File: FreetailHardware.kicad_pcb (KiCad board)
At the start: 2 copper layers, 51.5 x 41 mm, 50 parts, among them CON1 Transducer, J1 TX, J2 REF, J3 RX, Q1 S8050, U1 Teensy3.2, U2 LMV324

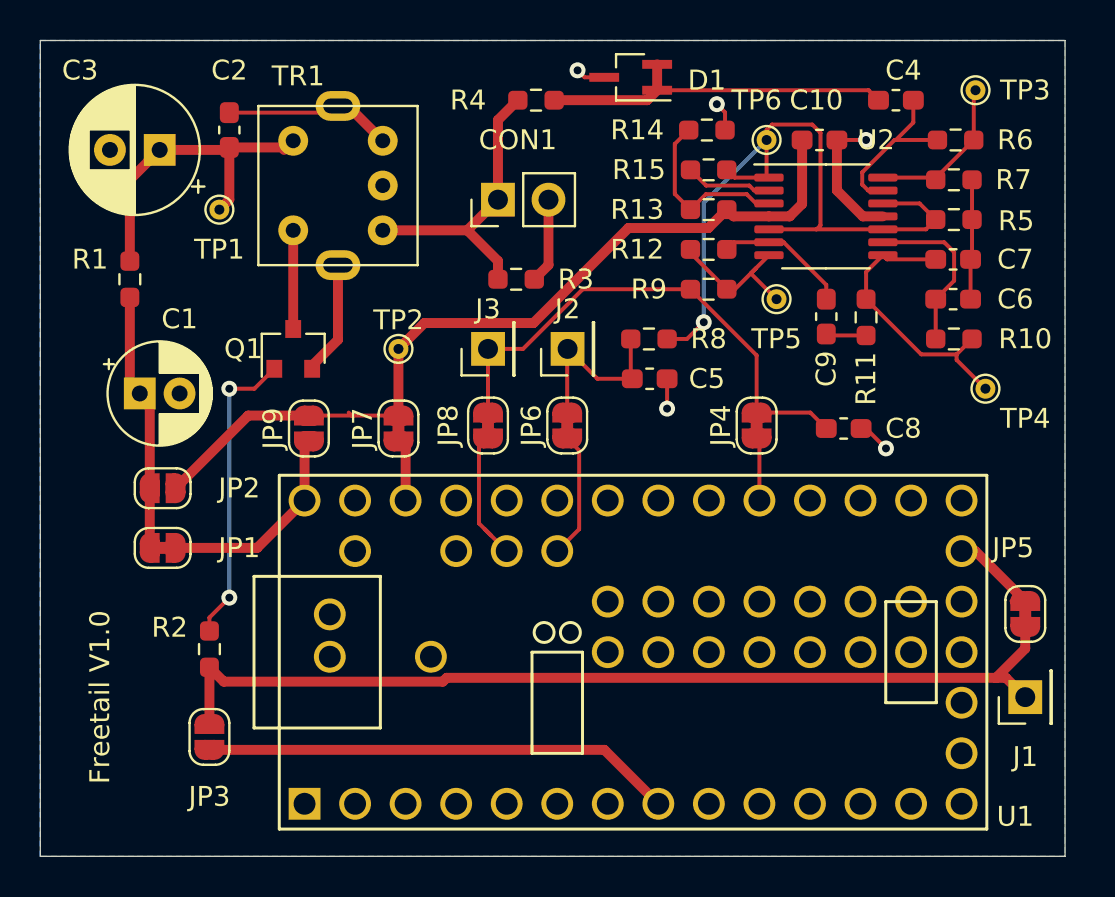
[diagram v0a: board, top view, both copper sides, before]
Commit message: Updated to KiCad v6
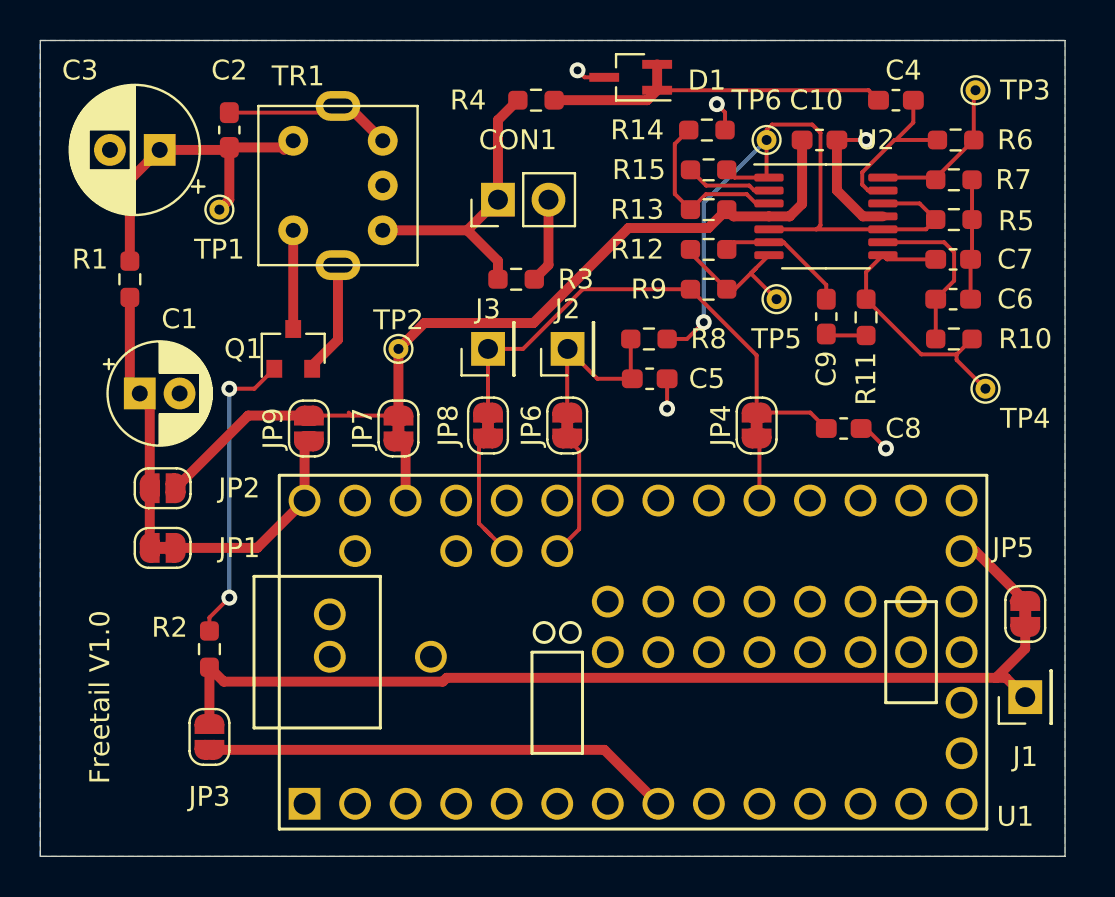
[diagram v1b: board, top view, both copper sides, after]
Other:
- net class Default removed

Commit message: v1.1 Hardware sent for fabrication
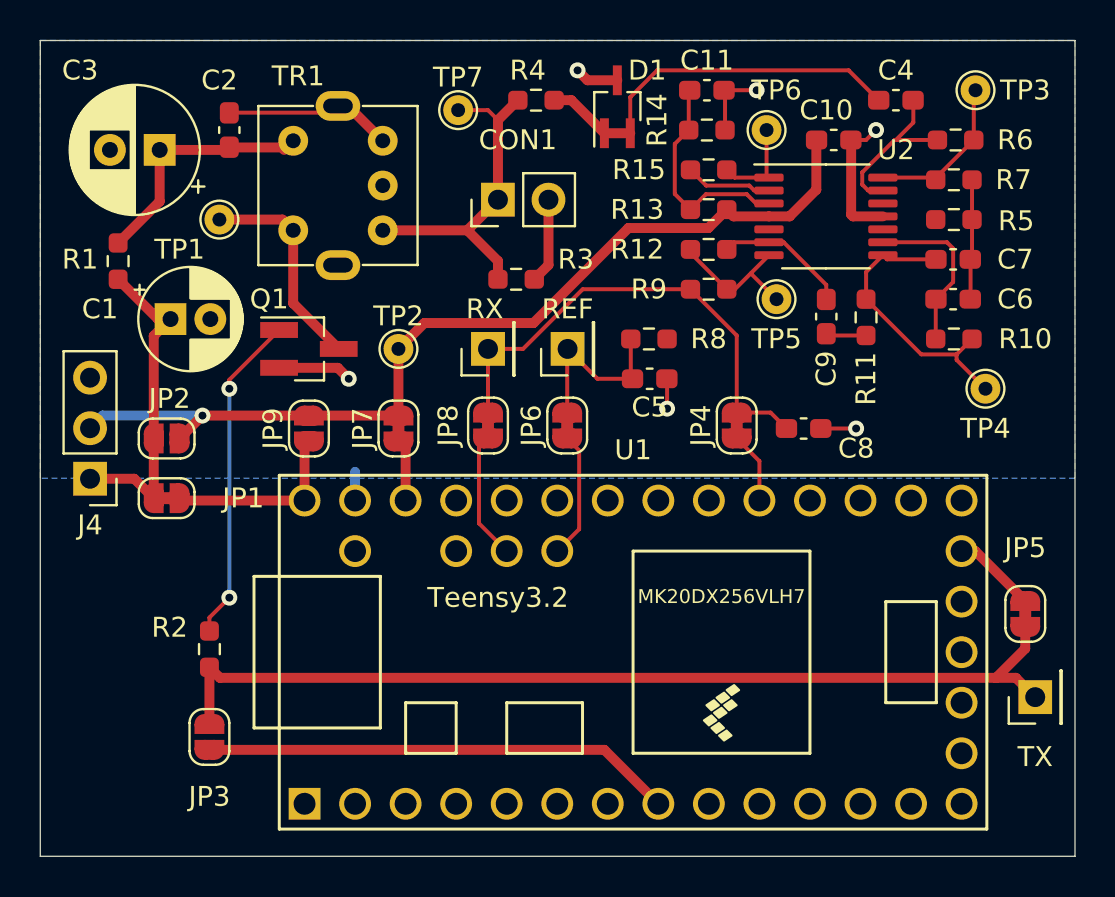
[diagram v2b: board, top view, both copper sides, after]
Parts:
- added C11: 100nF, Capacitor_SMD:C_0603_1608Metric_Pad1.08x0.95mm_HandSolder, F.Cu at (67.0, 23.5)
- added J4: Conn_01x03, Connector_PinHeader_2.54mm:PinHeader_1x03_P2.54mm_Vertical, F.Cu at (36.0, 43.0)
- added TP7: TestPoint, TestPoint:TestPoint_THTPad_D1.5mm_Drill0.7mm, F.Cu at (54.5, 24.5)
- C10, C2, C4, C5, C6, C7, C8, C9: footprint Capacitor_SMD:C_0603_1608Metric_Pad1.05x0.95mm_HandSolder -> Capacitor_SMD:C_0603_1608Metric_Pad1.08x0.95mm_HandSolder
- Q1: footprint Package_TO_SOT_SMD:SOT-23 -> Package_TO_SOT_SMD:SOT-23_Handsoldering
- R12: value 470k -> 56k
- TP1, TP2, TP3, TP4, TP5, TP6: footprint TestPoint:TestPoint_THTPad_D1.0mm_Drill0.5mm -> TestPoint:TestPoint_THTPad_D1.5mm_Drill0.7mm
- TR1: value 10:1 step-up 7-8nH secondary -> 10:1 step-up 7-8mH secondary
- U1: footprint teensy:Teensy30_31_32_All_Pins -> transformer:Teensy32
- moved Logo 20.9 mm to (69.5, 50.5)
- moved C1 4.05 mm to (40.0, 35.0)
- moved JP1 2.51 mm to (39.9, 44.0)
- moved JP2 2.51 mm to (39.9, 41.0)
- moved C8 2.01 mm to (71.9, 40.5)
- moved D1 1.62 mm to (62.5, 24.3), turned to 90 degrees
- moved R1 1.09 mm to (37.4, 32.1)
- moved JP4 1.00 mm to (68.5, 40.4)
- moved Q1 0.79 mm to (47.0, 36.5), turned to 0 degrees
- moved C10 0.72 mm to (73.4, 26.0)
- moved J1 0.50 mm to (83.5, 54.0)
- moved TP1 0.50 mm to (42.5, 30.0)
- moved TP6 0.50 mm to (70.0, 25.5)
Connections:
- net Net-(C1-Pad1) renamed /V_TX
- C1 pad 2: GND -> GNDA
- C10 pad 1: GND -> GNDA
- C2 pad 1: GND -> GNDA
- C3 pad 2: GND -> GNDA
- C5 pad 1: GND -> GNDA
- C8 pad 2: GND -> GNDA
- CON1 pad 2: GND -> GNDA
- D1 pad 3: GND -> GNDA
- Q1 pad 2: GND -> GNDA
- R14 pad 1: GND -> GNDA
- R15 pad 1: VCOM -> Net-(R15-Pad1)
- R3 pad 1: GND -> GNDA
- R5 pad 1: VCOM -> Net-(R5-Pad1)
- R8 pad 1: VCOM -> Net-(R8-Pad1)
- TP1 pad 1: Net-(C2-Pad2) -> Net-(Q1-Pad3)
- TP6 pad 1: VCOM -> Net-(R15-Pad1)
- TR1 pad 2: Net-(TR1-Pad2) -> unconnected-(TR1-Pad2)
- TR1 pad 3: GND -> GNDA
- TR1 pad 7: GND -> GNDA
- TR1 pad 8: GND -> GNDA
- U1 pad 1: GND -> unconnected-(U1-Pad1)
- U1 pad 10: Net-(U1-Pad10) -> unconnected-(U1-Pad10)
- U1 pad 11: Net-(U1-Pad11) -> unconnected-(U1-Pad11)
- U1 pad 12: Net-(U1-Pad12) -> unconnected-(U1-Pad12)
- U1 pad 13: Net-(U1-Pad13) -> unconnected-(U1-Pad13)
- U1 pad 14: Net-(U1-Pad14) -> unconnected-(U1-Pad14)
- U1 pad 15: Net-(U1-Pad15) -> unconnected-(U1-Pad15)
- U1 pad 16: Net-(U1-Pad16) -> unconnected-(U1-Pad16)
- U1 pad 17: Net-(U1-Pad17) -> unconnected-(U1-Pad17)
- U1 pad 18: Net-(U1-Pad18) -> unconnected-(U1-Pad18)
- U1 pad 2: Net-(U1-Pad2) -> unconnected-(U1-Pad2)
- U1 pad 20: Net-(U1-Pad20) -> unconnected-(U1-Pad20)
- U1 pad 21: Net-(U1-Pad21) -> unconnected-(U1-Pad21)
- U1 pad 22: Net-(U1-Pad22) -> unconnected-(U1-Pad22)
- U1 pad 23: Net-(U1-Pad23) -> unconnected-(U1-Pad23)
- U1 pad 25: Net-(U1-Pad25) -> unconnected-(U1-Pad25)
- U1 pad 26: Net-(U1-Pad26) -> unconnected-(U1-Pad26)
- U1 pad 27: Net-(U1-Pad27) -> unconnected-(U1-Pad27)
- U1 pad 28: Net-(U1-Pad28) -> unconnected-(U1-Pad28)
- U1 pad 29: Net-(U1-Pad29) -> unconnected-(U1-Pad29)
- U1 pad 3: Net-(U1-Pad3) -> unconnected-(U1-Pad3)
- U1 pad 30: Net-(U1-Pad30) -> unconnected-(U1-Pad30)
- U1 pad 32: Net-(U1-Pad32) -> GNDA
- U1 pad 34: Net-(U1-Pad34) -> unconnected-(U1-Pad34)
- U1 pad 35: Net-(U1-Pad35) -> unconnected-(U1-Pad35)
- U1 pad 4: Net-(U1-Pad4) -> unconnected-(U1-Pad4)
- U1 pad 5: Net-(U1-Pad5) -> unconnected-(U1-Pad5)
- U1 pad 6: Net-(U1-Pad6) -> unconnected-(U1-Pad6)
- U1 pad 7: Net-(U1-Pad7) -> unconnected-(U1-Pad7)
- U1 pad 9: Net-(U1-Pad9) -> unconnected-(U1-Pad9)
- U2 pad 1: VCOM -> Net-(R15-Pad1)
- U2 pad 10: VCOM -> Net-(U2-Pad10)
- U2 pad 11: GND -> GNDA
- U2 pad 12: VCOM -> Net-(U2-Pad12)
- U2 pad 5: VCOM -> Net-(U2-Pad5)
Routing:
- net VCOM: track 37.2 -> 0.00 mm, vias 1 -> 0
- net GNDA: track 0.00 -> 34.0 mm, vias 0 -> 6
- net GND: track 31.6 -> 0.00 mm, vias 5 -> 0
- net Net-(Q1-Pad3): track 4.96 -> 10.8 mm
- net VAA: track 43.1 -> 47.8 mm, vias 0 -> 1
- net Net-(R15-Pad1): track 0.00 -> 4.72 mm
- net Net-(C2-Pad2): track 17.1 -> 12.6 mm
- net /V_TX: track 13.0 -> 16.4 mm
- net Net-(CON1-Pad1): track 14.9 -> 17.1 mm
- net Net-(C11-Pad2): track 9.07 -> 11.1 mm
- net Net-(C4-Pad2): track 18.0 -> 20.0 mm
- net Net-(C8-Pad1): track 26.0 -> 24.6 mm
- net Net-(Q1-Pad1): track 15.3 -> 16.6 mm
- net +5V: track 10.5 -> 9.39 mm
- net Net-(JP8-Pad2): track 7.33 -> 6.43 mm
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- added copper zone on B.Cu, net GNDA
- removed copper zone on B.Cu, net GND
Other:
- board size 51.5 x 41 mm -> 52 x 41 mm
- board text added: "Freetail v1.1"
- board text added: "GNDA"
- board text added: "TP1 - TX transistor waveform TP2 - Analog supply voltage TP3 - first gain stage (high pass) TP4 - second gain stage (bandpass) TP5 - third gain stage (high pass) TP6 - half supply bias voltage TP7 - transducer waveform"
- board text added: "USB Plug"
- board text added: "VAA"
- board text added: "V_TX"
- board text removed: "Freetail V1.0"
- board text removed: "Freetail v1.0"

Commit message: Version 1.2 sent for fabrication Fix unconnected Vbias Mark soldered pads for Teensy Add capacitor for TX filter
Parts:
- added C12: Cfilt, Capacitor_SMD:C_0603_1608Metric_Pad1.08x0.95mm_HandSolder, F.Cu at (42.9, 46.9)
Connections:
- R15 pad 1: Net-(R15-Pad1) -> /Vbias
- R5 pad 1: Net-(R5-Pad1) -> /Vbias
- R8 pad 1: Net-(R8-Pad1) -> /Vbias
- TP6 pad 1: Net-(R15-Pad1) -> /Vbias
- U2 pad 1: Net-(R15-Pad1) -> /Vbias
- U2 pad 10: Net-(U2-Pad10) -> /Vbias
- U2 pad 12: Net-(U2-Pad12) -> /Vbias
- U2 pad 5: Net-(U2-Pad5) -> /Vbias
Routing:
- net /Vbias: track 0.00 -> 29.6 mm, vias 0 -> 3
- net GNDA: track 34.0 -> 39.3 mm
- net Net-(R15-Pad1): track 4.72 -> 0.00 mm
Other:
- board text added: "Freetail v1.2"
- board text removed: "Freetail v1.1"
